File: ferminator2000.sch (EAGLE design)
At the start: 120 parts, among them CN1 MINIB, IC1 FT232RL, IC2 REF01D, Q1 STP5NA50, Q2 STP5NA50, SW1 ENCODER_SW1-PEC12, U1 DSPIC33FJ256GP510A, U2 AD8495

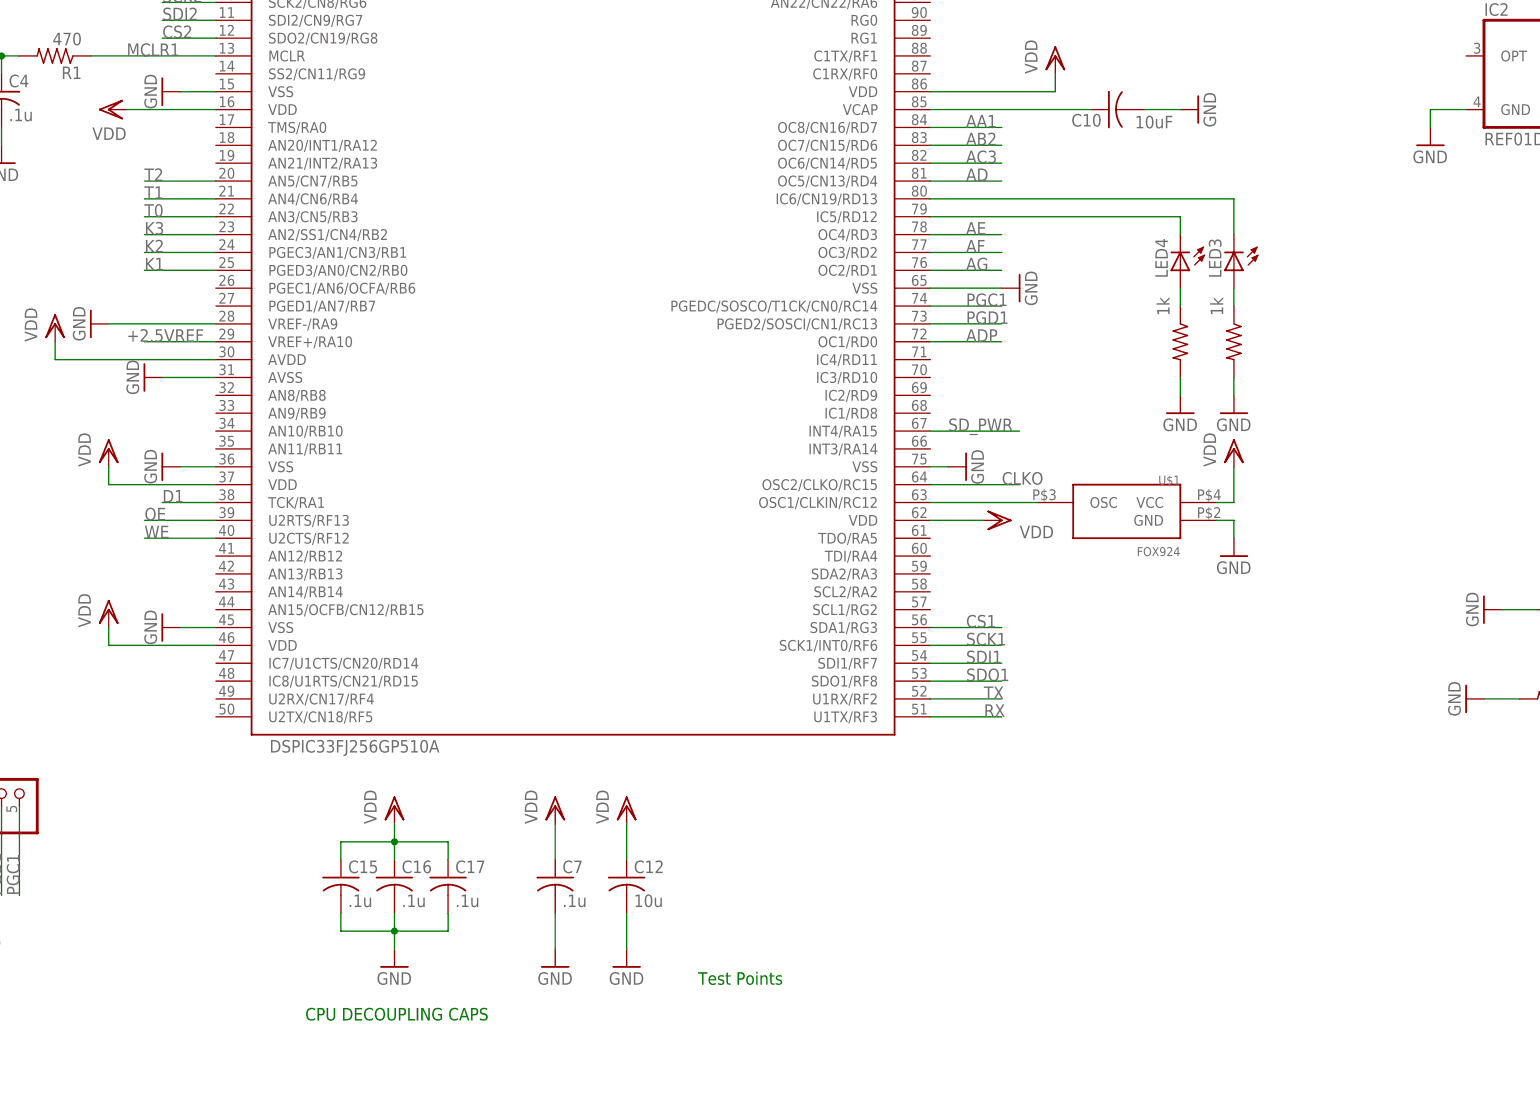
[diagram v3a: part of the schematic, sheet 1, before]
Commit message: Added RTC to hardware
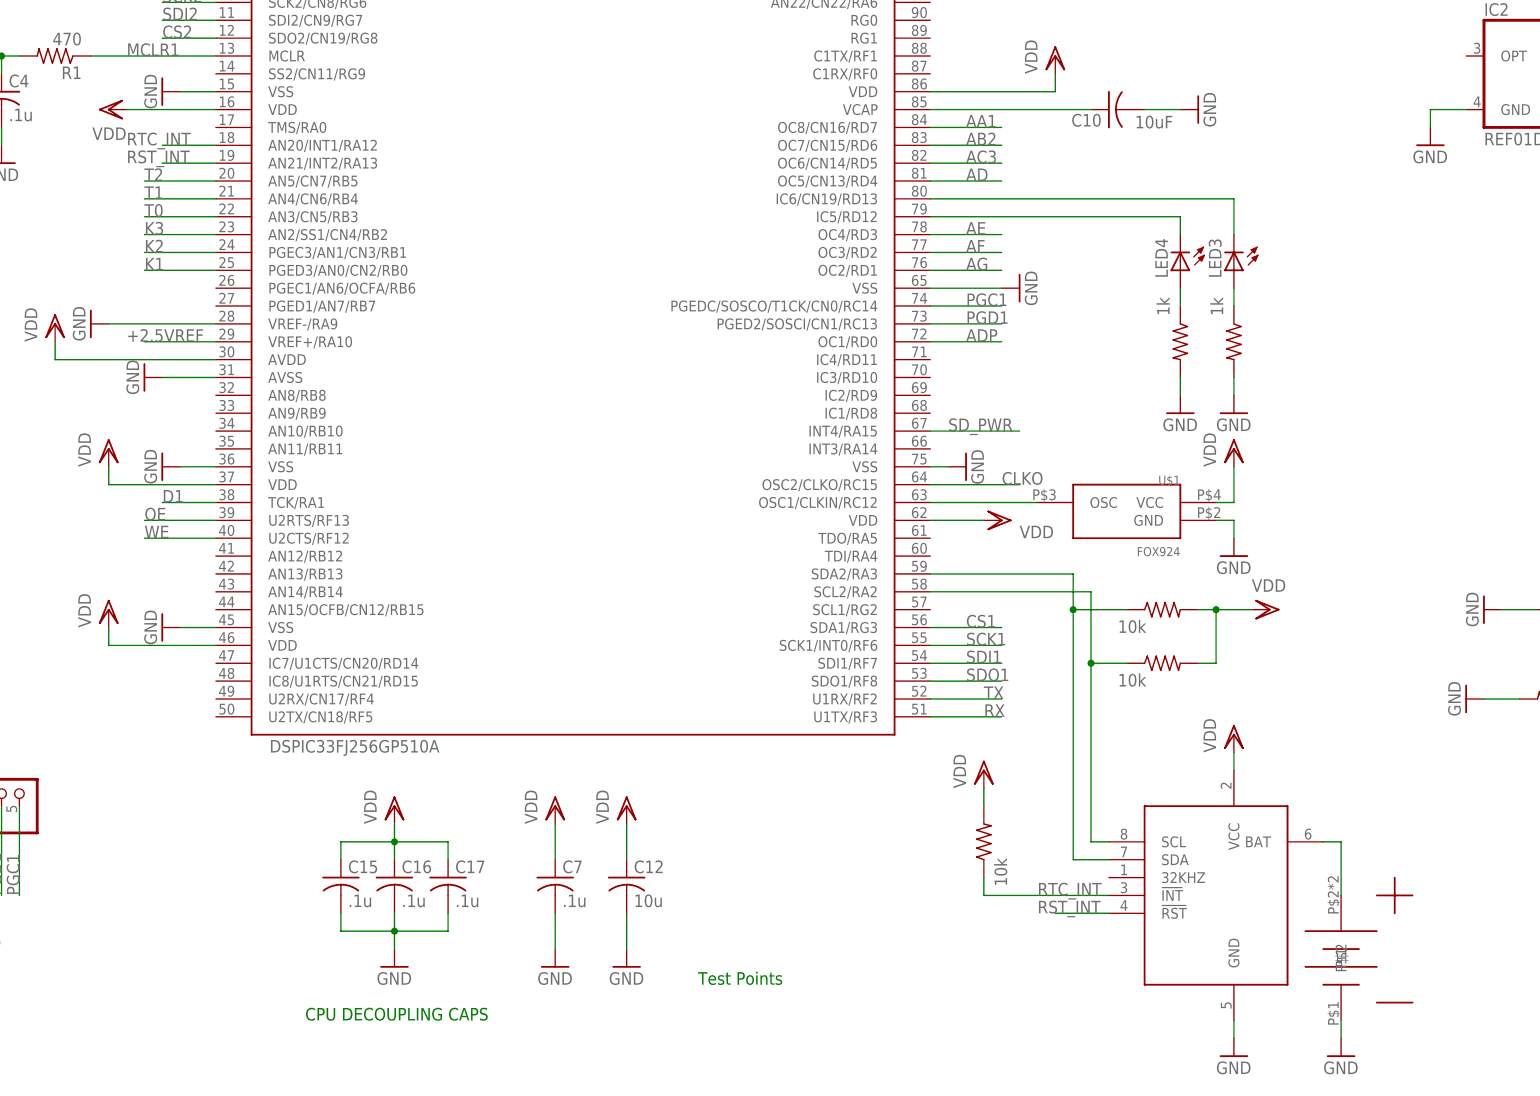
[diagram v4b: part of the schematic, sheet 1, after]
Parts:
- added R45, R53, R54: 10k, rcl:R-US_R0805
- added U$2: 12MM_BATTER_HOLDER, eric_sorensen:12MM_BATTER_HOLDER
- added U$5: DS3231, eric_sorensen:DS3231
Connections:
- new net N$22: U$2.P$1, U$5.BAT
- new net N$23: R45.1, U$5.SDA, U1.SDA2/RA3
- new net N$60: R53.1, U$5.SCL, U1.SCL2/RA2
- new net RST_INT: U$5.!RST, U1.AN21/INT2/RA13
- new net RTC_INT: R54.1, U$5.!INT, U1.AN20/INT1/RA12
- net GND: now also U$2.P$2, U$5.GND
- net VDD: now also R45.2, R53.2, R54.2, U$5.VCC
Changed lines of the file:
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@@
 <part name="P+7" library="supply1" deviceset="+24V" device=""/>
 <part name="GND5" library="supply1" deviceset="GND" device=""/>
+<part name="U$2" library="eric_sorensen" deviceset="12MM_BATTER_HOLDER" device=""/>
+<part name="GND33" library="supply1" deviceset="GND" device=""/>
+<part name="U$5" library="eric_sorensen" deviceset="DS3231" device=""/>
+<part name="GND42" library="supply1" deviceset="GND" device=""/>
+<part name="VDD19" library="supply1" deviceset="VDD" device=""/>
+<part name="R45" library="rcl" deviceset="R-US_" device="R0805" value="10k"/>
+<part name="R53" library="rcl" deviceset="R-US_" device="R0805" value="10k"/>
+<part name="VDD21" library="supply1" deviceset="VDD" device=""/>
+<part name="R54" library="rcl" deviceset="R-US_" device="R0805" value="10k"/>
+<part name="VDD22" library="supply1" deviceset="VDD" device=""/>
 </parts>
 <sheets>
@@
 <instance part="GND4" gate="1" x="325.12" y="22.86"/>
 <instance part="VDD9" gate="G$1" x="314.96" y="33.02"/>
+<instance part="U$2" gate="G$1" x="518.16" y="17.78"/>
+<instance part="GND33" gate="1" x="518.16" y="5.08"/>
+<instance part="U$5" gate="G$1" x="492.76" y="20.32"/>
+<instance part="GND42" gate="1" x="502.92" y="5.08"/>
+<instance part="VDD19" gate="G$1" x="502.92" y="50.8"/>
+<instance part="R45" gate="G$1" x="492.76" y="68.58" smashed="yes">
+<attribute name="VALUE" x="486.41" y="65.278" size="1.778" layer="96"/>
+</instance>
+<instance part="R53" gate="G$1" x="492.76" y="60.96" smashed="yes">
+<attribute name="VALUE" x="486.41" y="57.658" size="1.778" layer="96"/>
+</instance>
+<instance part="VDD21" gate="G$1" x="508" y="68.58" rot="R270"/>
+<instance part="R54" gate="G$1" x="467.36" y="35.56" smashed="yes" rot="R90">
+<attribute name="VALUE" x="470.662" y="29.21" size="1.778" layer="96" rot="R90"/>
+</instance>
+<instance part="VDD22" gate="G$1" x="467.36" y="45.72"/>
 </instances>
 <busses>
@@
 <pinref part="VDD9" gate="G$1" pin="VDD"/>
 </segment>
+<segment>
+<pinref part="U$5" gate="G$1" pin="VCC"/>
+<pinref part="VDD19" gate="G$1" pin="VDD"/>
+<wire x1="502.92" y1="45.72" x2="502.92" y2="48.26" width="0.1524" layer="91"/>
+</segment>
+<segment>
+<pinref part="VDD21" gate="G$1" pin="VDD"/>
+<pinref part="R45" gate="G$1" pin="2"/>
+<wire x1="505.46" y1="68.58" x2="500.38" y2="68.58" width="0.1524" layer="91"/>
+<pinref part="R53" gate="G$1" pin="2"/>
+<wire x1="500.38" y1="68.58" x2="497.84" y2="68.58" width="0.1524" layer="91"/>
+<wire x1="497.84" y1="60.96" x2="500.38" y2="60.96" width="0.1524" layer="91"/>
+<wire x1="500.38" y1="60.96" x2="500.38" y2="68.58" width="0.1524" layer="91"/>
+<junction x="500.38" y="68.58"/>
+</segment>
+<segment>
+<pinref part="R54" gate="G$1" pin="2"/>
+<wire x1="467.36" y1="40.64" x2="467.36" y2="43.18" width="0.1524" layer="91"/>
+<pinref part="VDD22" gate="G$1" pin="VDD"/>
+</segment>
 </net>
 <net name="GND" class="0">
@@
 <pinref part="GND4" gate="1" pin="GND"/>
 </segment>
+<segment>
+<pinref part="GND33" gate="1" pin="GND"/>
+<pinref part="U$2" gate="G$1" pin="P$2"/>
+<wire x1="518.16" y1="7.62" x2="518.16" y2="10.16" width="0.1524" layer="91"/>
+</segment>
+<segment>
+<pinref part="GND42" gate="1" pin="GND"/>
+<pinref part="U$5" gate="G$1" pin="GND"/>
+<wire x1="502.92" y1="7.62" x2="502.92" y2="10.16" width="0.1524" layer="91"/>
+</segment>
 </net>
 <net name="PGD1" class="0">
@@
 </segment>
 </net>
+<net name="N$22" class="0">
+<segment>
+<pinref part="U$5" gate="G$1" pin="BAT"/>
+<wire x1="515.62" y1="35.56" x2="518.16" y2="35.56" width="0.1524" layer="91"/>
+<pinref part="U$2" gate="G$1" pin="P$1"/>
+<wire x1="518.16" y1="35.56" x2="518.16" y2="27.94" width="0.1524" layer="91"/>
+</segment>
+</net>
+<net name="N$23" class="0">
+<segment>
+<pinref part="U1" gate="G$1" pin="SDA2/RA3"/>
+<wire x1="459.74" y1="73.66" x2="480.06" y2="73.66" width="0.1524" layer="91"/>
+<wire x1="480.06" y1="73.66" x2="480.06" y2="68.58" width="0.1524" layer="91"/>
+<pinref part="U$5" gate="G$1" pin="SDA"/>
+<wire x1="480.06" y1="68.58" x2="480.06" y2="33.02" width="0.1524" layer="91"/>
+<wire x1="480.06" y1="33.02" x2="485.14" y2="33.02" width="0.1524" layer="91"/>
+<pinref part="R45" gate="G$1" pin="1"/>
+<wire x1="487.68" y1="68.58" x2="480.06" y2="68.58" width="0.1524" layer="91"/>
+<junction x="480.06" y="68.58"/>
+</segment>
+</net>
+<net name="N$60" class="0">
+<segment>
+<pinref part="U1" gate="G$1" pin="SCL2/RA2"/>
+<wire x1="459.74" y1="71.12" x2="482.6" y2="71.12" width="0.1524" layer="91"/>
+<wire x1="482.6" y1="71.12" x2="482.6" y2="60.96" width="0.1524" layer="91"/>
+<pinref part="U$5" gate="G$1" pin="SCL"/>
+<wire x1="482.6" y1="60.96" x2="482.6" y2="35.56" width="0.1524" layer="91"/>
+<wire x1="482.6" y1="35.56" x2="485.14" y2="35.56" width="0.1524" layer="91"/>
+<pinref part="R53" gate="G$1" pin="1"/>
+<wire x1="487.68" y1="60.96" x2="482.6" y2="60.96" width="0.1524" layer="91"/>
+<junction x="482.6" y="60.96"/>
+</segment>
+</net>
+<net name="RTC_INT" class="0">
+<segment>
+<pinref part="U$5" gate="G$1" pin="!INT"/>
+<label x="474.98" y="27.94" size="1.778" layer="95"/>
+<pinref part="R54" gate="G$1" pin="1"/>
+<wire x1="485.14" y1="27.94" x2="467.36" y2="27.94" width="0.1524" layer="91"/>
+<wire x1="467.36" y1="27.94" x2="467.36" y2="30.48" width="0.1524" layer="91"/>
+</segment>
+<segment>
+<pinref part="U1" gate="G$1" pin="AN20/INT1/RA12"/>
+<wire x1="358.14" y1="134.62" x2="350.52" y2="134.62" width="0.1524" layer="91"/>
+<label x="345.44" y="134.62" size="1.778" layer="95"/>
+</segment>
+</net>
+<net name="RST_INT" class="0">
+<segment>
+<pinref part="U$5" gate="G$1" pin="!RST"/>
+<wire x1="485.14" y1="25.4" x2="477.52" y2="25.4" width="0.1524" layer="91"/>
+<label x="474.98" y="25.4" size="1.778" layer="95"/>
+</segment>
+<segment>
+<pinref part="U1" gate="G$1" pin="AN21/INT2/RA13"/>
+<wire x1="358.14" y1="132.08" x2="350.52" y2="132.08" width="0.1524" layer="91"/>
+<label x="345.44" y="132.08" size="1.778" layer="95"/>
+</segment>
+</net>

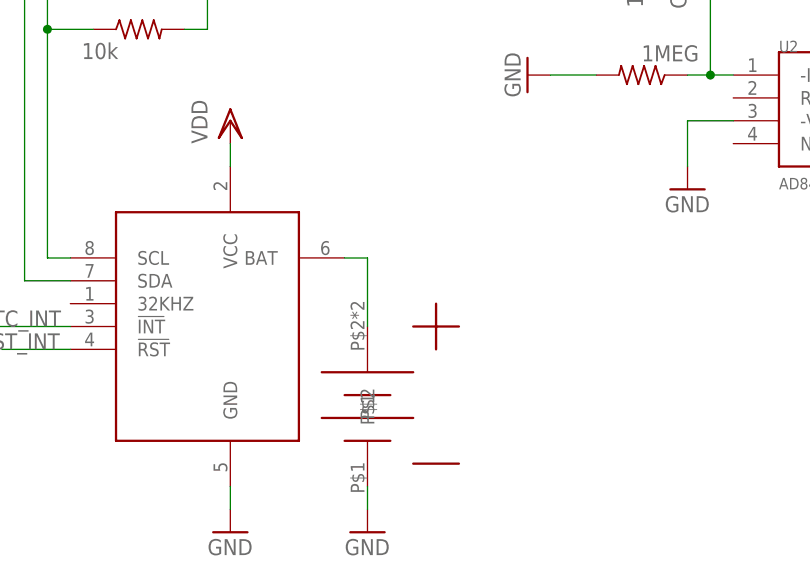
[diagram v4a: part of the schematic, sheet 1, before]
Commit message: Added 0.1uF decoupling cap to RTC
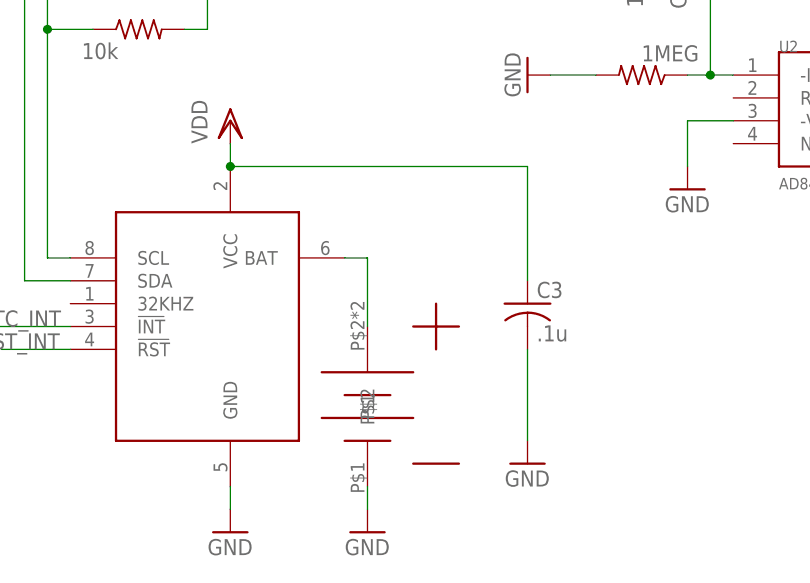
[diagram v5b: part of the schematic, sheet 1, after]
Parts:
- added C3: .1u, rcl:C-USC0603
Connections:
- net GND: now also C3.2
- net VDD: now also C3.1
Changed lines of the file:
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@@
 <part name="R54" library="rcl" deviceset="R-US_" device="R0805" value="10k"/>
 <part name="VDD22" library="supply1" deviceset="VDD" device=""/>
+<part name="C3" library="rcl" deviceset="C-US" device="C0603" value=".1u"/>
+<part name="GND45" library="supply1" deviceset="GND" device=""/>
 </parts>
 <sheets>
@@
 </instance>
 <instance part="VDD22" gate="G$1" x="467.36" y="45.72"/>
+<instance part="C3" gate="G$1" x="535.94" y="30.48"/>
+<instance part="GND45" gate="1" x="535.94" y="12.7"/>
 </instances>
 <busses>
@@
 <pinref part="VDD19" gate="G$1" pin="VDD"/>
 <wire x1="502.92" y1="45.72" x2="502.92" y2="48.26" width="0.1524" layer="91"/>
+<pinref part="C3" gate="G$1" pin="1"/>
+<wire x1="502.92" y1="45.72" x2="535.94" y2="45.72" width="0.1524" layer="91"/>
+<wire x1="535.94" y1="45.72" x2="535.94" y2="33.02" width="0.1524" layer="91"/>
+<junction x="502.92" y="45.72"/>
 </segment>
 <segment>
@@
 <wire x1="502.92" y1="7.62" x2="502.92" y2="10.16" width="0.1524" layer="91"/>
 </segment>
+<segment>
+<pinref part="C3" gate="G$1" pin="2"/>
+<wire x1="535.94" y1="25.4" x2="535.94" y2="15.24" width="0.1524" layer="91"/>
+<pinref part="GND45" gate="1" pin="GND"/>
+</segment>
 </net>

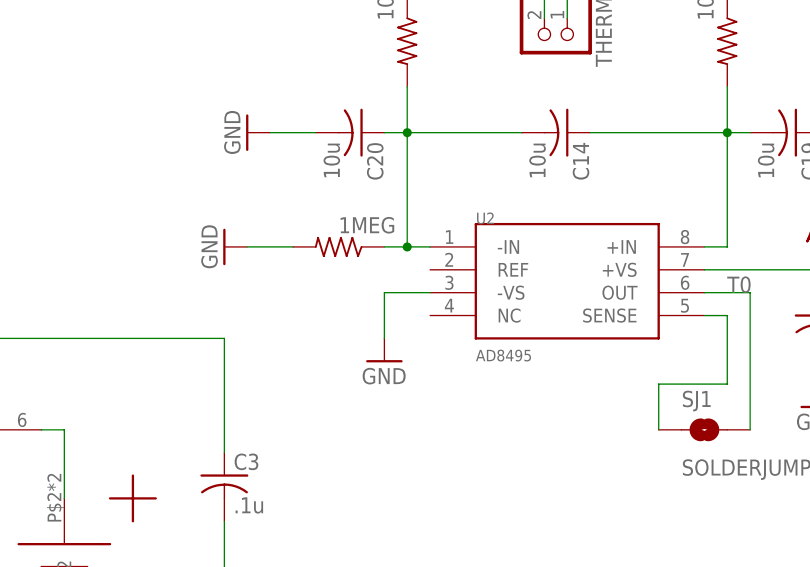
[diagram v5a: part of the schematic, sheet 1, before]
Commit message: Tied REF pin of AD8495 (thermocouple driver) to ground
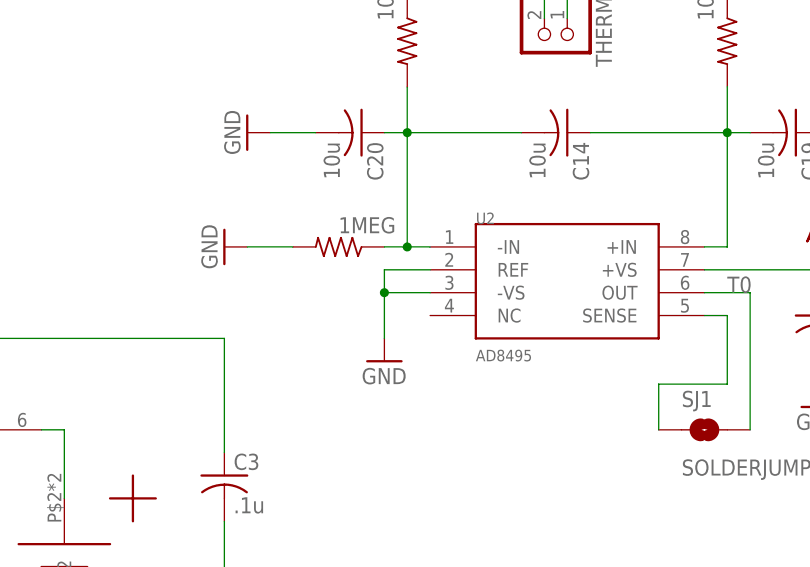
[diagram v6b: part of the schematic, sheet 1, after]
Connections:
- net GND: now also U2.REF
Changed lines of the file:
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@@
 <pinref part="U2" gate="G$1" pin="-VS"/>
 <wire x1="553.72" y1="50.8" x2="558.8" y2="50.8" width="0.1524" layer="91"/>
+<pinref part="U2" gate="G$1" pin="REF"/>
+<wire x1="558.8" y1="53.34" x2="553.72" y2="53.34" width="0.1524" layer="91"/>
+<wire x1="553.72" y1="53.34" x2="553.72" y2="50.8" width="0.1524" layer="91"/>
+<junction x="553.72" y="50.8"/>
 </segment>
 <segment>
